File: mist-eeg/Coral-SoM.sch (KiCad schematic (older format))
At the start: 20 parts, among them J5 Extra GPIOs, J6 Digital buses, J7 J1312, J8 J1311, J9 J1310, SW4 RESET, SW5 ONOFF, U9 NX5427001Z

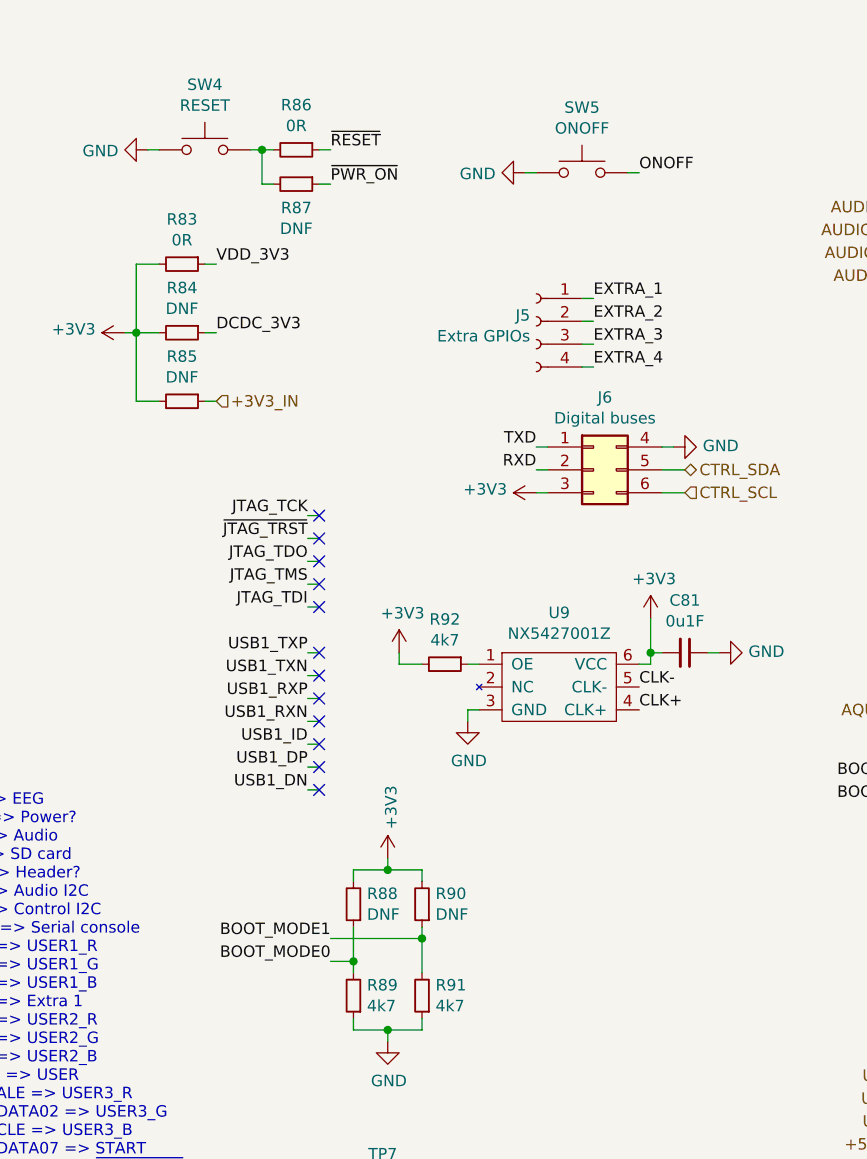
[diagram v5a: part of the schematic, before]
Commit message: Switch to POL switching regulator to accelerate production of the board
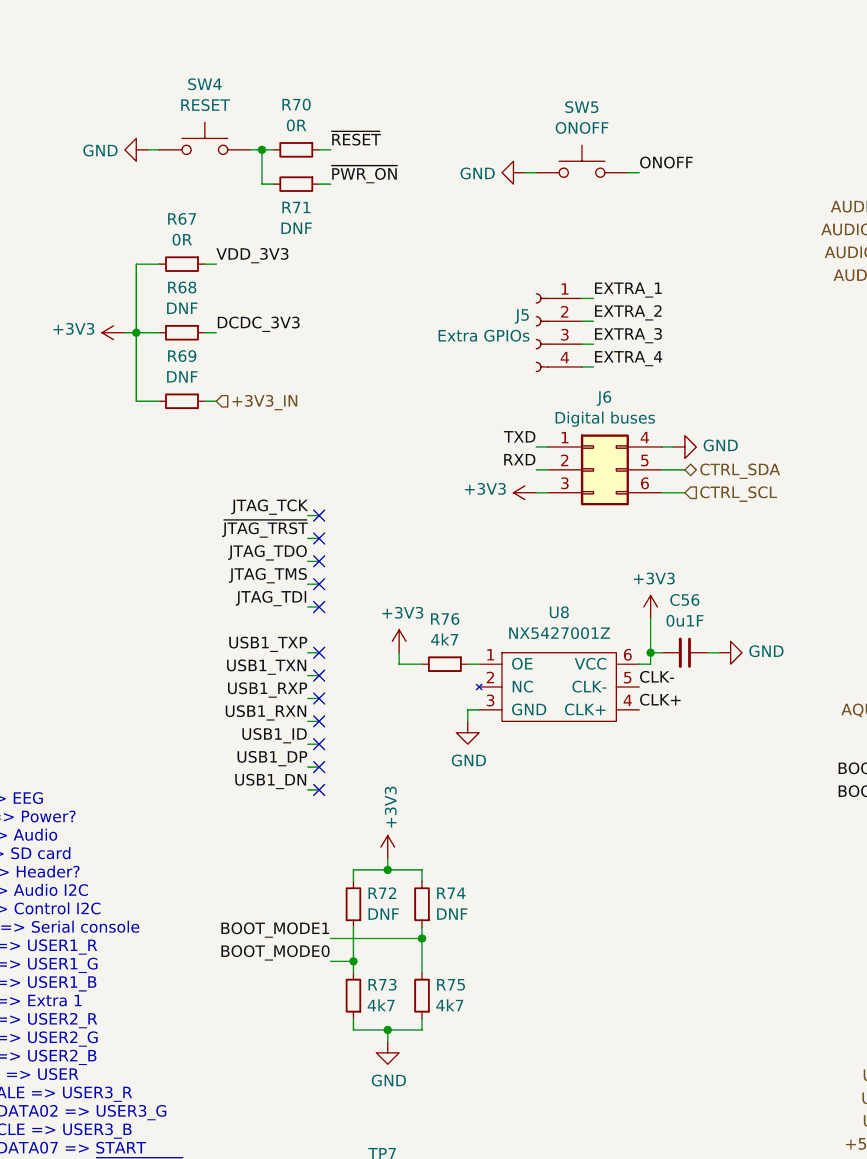
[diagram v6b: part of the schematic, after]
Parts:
- renumbered C81 to C56, R83 to R67, R84 to R68, R85 to R69, R86 to R70, R87 to R71, R88 to R72, R89 to R73, R90 to R74, R91 to R75, R92 to R76, U9 to U8
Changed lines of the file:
@@
 $Descr A4 11693 8268
 encoding utf-8
-Sheet 11 11
+Sheet 11 8
 Title ""
-Date "2021-08-03"
-Rev "1D"
+Date "2021-08-05"
+Rev "1E"
 Comp ""
 Comment1 ""
@@
 $EndComp
 $Comp
-L power:GND #PWR0113
+L power:GND #PWR091
 U 1 1 614447D0
 P 5050 6000
-F 0 "#PWR0113" H 5050 5750 50  0001 C CNN
+F 0 "#PWR091" H 5050 5750 50  0001 C CNN
 F 1 "GND" H 5055 5827 50  0000 C CNN
 F 2 "" H 5050 6000 50  0001 C CNN
@@
 $EndComp
 $Comp
-L power:GND #PWR0114
+L power:GND #PWR092
 U 1 1 61444C99
 P 5450 6000
-F 0 "#PWR0114" H 5450 5750 50  0001 C CNN
+F 0 "#PWR092" H 5450 5750 50  0001 C CNN
 F 1 "GND" H 5455 5827 50  0000 C CNN
 F 2 "" H 5450 6000 50  0001 C CNN
@@
 $EndComp
 $Comp
-L power:GND #PWR0115
+L power:GND #PWR093
 U 1 1 61445116
 P 7050 5950
-F 0 "#PWR0115" H 7050 5700 50  0001 C CNN
+F 0 "#PWR093" H 7050 5700 50  0001 C CNN
 F 1 "GND" H 7055 5777 50  0000 C CNN
 F 2 "" H 7050 5950 50  0001 C CNN
@@
 $EndComp
 $Comp
-L power:GND #PWR0116
+L power:GND #PWR094
 U 1 1 6144559F
 P 7450 5950
-F 0 "#PWR0116" H 7450 5700 50  0001 C CNN
+F 0 "#PWR094" H 7450 5700 50  0001 C CNN
 F 1 "GND" H 7455 5777 50  0000 C CNN
 F 2 "" H 7450 5950 50  0001 C CNN
@@
 $EndComp
 $Comp
-L power:GND #PWR0117
+L power:GND #PWR095
 U 1 1 61445A23
 P 9850 5950
-F 0 "#PWR0117" H 9850 5700 50  0001 C CNN
+F 0 "#PWR095" H 9850 5700 50  0001 C CNN
 F 1 "GND" H 9855 5777 50  0000 C CNN
 F 2 "" H 9850 5950 50  0001 C CNN
@@
 $EndComp
 $Comp
-L power:GND #PWR0118
+L power:GND #PWR096
 U 1 1 61445EC4
 P 10250 5950
-F 0 "#PWR0118" H 10250 5700 50  0001 C CNN
+F 0 "#PWR096" H 10250 5700 50  0001 C CNN
 F 1 "GND" H 10255 5777 50  0000 C CNN
 F 2 "" H 10250 5950 50  0001 C CNN
@@
 Connection ~ 5500 5600
 $Comp
-L power:+3V3 #PWR0102
+L power:+3V3 #PWR080
 U 1 1 615CEE3B
 P 1400 2050
-F 0 "#PWR0102" H 1400 1900 50  0001 C CNN
+F 0 "#PWR080" H 1400 1900 50  0001 C CNN
 F 1 "+3V3" V 1415 2178 50  0000 L CNN
 F 2 "" H 1400 2050 50  0001 C CNN
@@
 P 1500 1250
 AR Path="/60D119DF/616B49C1" Ref="#PWR?"  Part="1"
-AR Path="/61085AB7/616B49C1" Ref="#PWR0103"  Part="1"
-F 0 "#PWR0103" H 1500 1000 50  0001 C CNN
+AR Path="/61085AB7/616B49C1" Ref="#PWR081"  Part="1"
+F 0 "#PWR081" H 1500 1000 50  0001 C CNN
 F 1 "GND" V 1505 1122 50  0000 R CNN
 F 2 "" H 1500 1250 50  0001 C CNN
@@
 +3V3_IN
 $Comp
-L Device:R_Small R83
+L Device:R_Small R67
 U 1 1 60FDBF94
 P 1650 1750
-F 0 "R83" V 1454 1750 50  0000 C CNN
+F 0 "R67" V 1454 1750 50  0000 C CNN
 F 1 "0R" V 1545 1750 50  0000 C CNN
 F 2 "Resistor_SMD:R_0603_1608Metric" H 1650 1750 50  0001 C CNN
@@
 $EndComp
 $Comp
-L Device:R_Small R84
+L Device:R_Small R68
 U 1 1 60FDC090
 P 1650 2050
-F 0 "R84" V 1454 2050 50  0000 C CNN
+F 0 "R68" V 1454 2050 50  0000 C CNN
 F 1 "DNF" V 1545 2050 50  0000 C CNN
 F 2 "Resistor_SMD:R_0603_1608Metric" H 1650 2050 50  0001 C CNN
@@
 $EndComp
 $Comp
-L Device:R_Small R85
+L Device:R_Small R69
 U 1 1 60FDC0FE
 P 1650 2350
-F 0 "R85" V 1454 2350 50  0000 C CNN
+F 0 "R69" V 1454 2350 50  0000 C CNN
 F 1 "DNF" V 1545 2350 50  0000 C CNN
 F 2 "Resistor_SMD:R_0603_1608Metric" H 1650 2350 50  0001 C CNN
@@
 	3200 2750 3250 2750
 $Comp
-L power:+3V3 #PWR0109
+L power:+3V3 #PWR087
 U 1 1 627DB411
 P 3200 2750
-F 0 "#PWR0109" H 3200 2600 50  0001 C CNN
+F 0 "#PWR087" H 3200 2600 50  0001 C CNN
 F 1 "+3V3" V 3215 2878 50  0000 L CNN
 F 2 "" H 3200 2750 50  0001 C CNN
@@
 $EndComp
 $Comp
-L power:GND #PWR0111
+L power:GND #PWR089
 U 1 1 627DBA20
 P 3800 2550
-F 0 "#PWR0111" H 3800 2300 50  0001 C CNN
+F 0 "#PWR089" H 3800 2300 50  0001 C CNN
 F 1 "GND" V 3805 2422 50  0000 R CNN
 F 2 "" H 3800 2550 50  0001 C CNN
@@
 NoConn ~ 9900 2400
 $Comp
-L Device:R_Small R89
+L Device:R_Small R73
 U 1 1 6290419F
 P 2400 4950
-F 0 "R89" H 2341 4904 50  0000 R CNN
+F 0 "R73" H 2341 4904 50  0000 R CNN
 F 1 "4k7" H 2341 4995 50  0000 R CNN
 F 2 "Resistor_SMD:R_0201_0603Metric" H 2400 4950 50  0001 C CNN
@@
 $EndComp
 $Comp
-L Device:R_Small R91
+L Device:R_Small R75
 U 1 1 6290451A
 P 2700 4950
-F 0 "R91" H 2641 4904 50  0000 R CNN
+F 0 "R75" H 2641 4904 50  0000 R CNN
 F 1 "4k7" H 2641 4995 50  0000 R CNN
 F 2 "Resistor_SMD:R_0201_0603Metric" H 2700 4950 50  0001 C CNN
@@
 $EndComp
 $Comp
-L Device:R_Small R90
+L Device:R_Small R74
 U 1 1 62905418
 P 2700 4550
-F 0 "R90" H 2641 4504 50  0000 R CNN
+F 0 "R74" H 2641 4504 50  0000 R CNN
 F 1 "DNF" H 2641 4595 50  0000 R CNN
 F 2 "Resistor_SMD:R_0603_1608Metric" H 2700 4550 50  0001 C CNN
@@
 $EndComp
 $Comp
-L Device:R_Small R88
+L Device:R_Small R72
 U 1 1 62905675
 P 2400 4550
-F 0 "R88" H 2341 4504 50  0000 R CNN
+F 0 "R72" H 2341 4504 50  0000 R CNN
 F 1 "DNF" H 2341 4595 50  0000 R CNN
 F 2 "Resistor_SMD:R_0603_1608Metric" H 2400 4550 50  0001 C CNN
@@
 	2700 4400 2700 4450
 $Comp
-L power:GND #PWR0105
+L power:GND #PWR083
 U 1 1 629D21D1
 P 2550 5150
-F 0 "#PWR0105" H 2550 4900 50  0001 C CNN
+F 0 "#PWR083" H 2550 4900 50  0001 C CNN
 F 1 "GND" H 2555 4977 50  0000 C CNN
 F 2 "" H 2550 5150 50  0001 C CNN
@@
 	2000 1250 2050 1250
 $Comp
-L Device:R_Small R86
+L Device:R_Small R70
 U 1 1 62ADCC1F
 P 2150 1250
-F 0 "R86" V 1954 1250 50  0000 C CNN
+F 0 "R70" V 1954 1250 50  0000 C CNN
 F 1 "0R" V 2045 1250 50  0000 C CNN
 F 2 "Resistor_SMD:R_0603_1608Metric" H 2150 1250 50  0001 C CNN
@@
 $EndComp
 $Comp
-L Device:R_Small R87
+L Device:R_Small R71
 U 1 1 62ADCD0B
 P 2150 1400
-F 0 "R87" V 2254 1400 50  0000 C CNN
+F 0 "R71" V 2254 1400 50  0000 C CNN
 F 1 "DNF" V 2345 1400 50  0000 C CNN
 F 2 "Resistor_SMD:R_0603_1608Metric" H 2150 1400 50  0001 C CNN
@@
 	3650 1350 3600 1350
 $Comp
-L power:GND #PWR0108
+L power:GND #PWR086
 U 1 1 62B8A22D
 P 3150 1350
-F 0 "#PWR0108" H 3150 1100 50  0001 C CNN
+F 0 "#PWR086" H 3150 1100 50  0001 C CNN
 F 1 "GND" V 3155 1222 50  0000 R CNN
 F 2 "" H 3150 1350 50  0001 C CNN
@@
 	3150 1350 3200 1350
 $Comp
-L components:NX5427001Z U9
+L components:NX5427001Z U8
 U 1 1 6103BE94
 P 3250 3600
-F 0 "U9" H 3300 3925 50  0000 C CNN
+F 0 "U8" H 3300 3925 50  0000 C CNN
 F 1 "NX5427001Z" H 3300 3834 50  0000 C CNN
 F 2 "mist-eeg:NX5427001Z" H 3250 3500 50  0001 C CNN
@@
 CLK+
 $Comp
-L power:+3V3 #PWR0110
+L power:+3V3 #PWR088
 U 1 1 610A4550
 P 3700 3300
-F 0 "#PWR0110" H 3700 3150 50  0001 C CNN
+F 0 "#PWR088" H 3700 3150 50  0001 C CNN
 F 1 "+3V3" H 3715 3473 50  0000 C CNN
 F 2 "" H 3700 3300 50  0001 C CNN
@@
 	3700 3500 3650 3500
 $Comp
-L Device:C_Small C81
+L Device:C_Small C56
 U 1 1 610C70CD
 P 3850 3450
-F 0 "C81" V 3621 3450 50  0000 C CNN
+F 0 "C56" V 3621 3450 50  0000 C CNN
 F 1 "0u1F" V 3712 3450 50  0000 C CNN
 F 2 "Capacitor_SMD:C_0201_0603Metric" H 3850 3450 50  0001 C CNN
@@
 	3700 3450 3700 3500
 $Comp
-L power:GND #PWR0112
+L power:GND #PWR090
 U 1 1 610E9DBB
 P 4000 3450
-F 0 "#PWR0112" H 4000 3200 50  0001 C CNN
+F 0 "#PWR090" H 4000 3200 50  0001 C CNN
 F 1 "GND" V 4005 3322 50  0000 R CNN
 F 2 "" H 4000 3450 50  0001 C CNN
@@
 	4000 3450 3950 3450
 $Comp
-L power:GND #PWR0107
+L power:GND #PWR085
 U 1 1 611314F6
 P 2900 3750
-F 0 "#PWR0107" H 2900 3500 50  0001 C CNN
+F 0 "#PWR085" H 2900 3500 50  0001 C CNN
 F 1 "GND" H 2905 3577 50  0000 C CNN
 F 2 "" H 2900 3750 50  0001 C CNN
@@
 	2900 3700 2950 3700
 $Comp
-L Device:R_Small R92
+L Device:R_Small R76
 U 1 1 61156BB0
 P 2800 3500
-F 0 "R92" V 2604 3500 50  0000 C CNN
+F 0 "R76" V 2604 3500 50  0000 C CNN
 F 1 "4k7" V 2695 3500 50  0000 C CNN
 F 2 "Resistor_SMD:R_0201_0603Metric" H 2800 3500 50  0001 C CNN
@@
 $EndComp
 $Comp
-L power:+3V3 #PWR0106
+L power:+3V3 #PWR084
 U 1 1 61157269
 P 2600 3450
-F 0 "#PWR0106" H 2600 3300 50  0001 C CNN
+F 0 "#PWR084" H 2600 3300 50  0001 C CNN
 F 1 "+3V3" H 2615 3623 50  0000 C CNN
 F 2 "" H 2600 3450 50  0001 C CNN
@@
 	2600 3500 2700 3500
 $Comp
-L power:+3V3 #PWR0104
+L power:+3V3 #PWR082
 U 1 1 6104B8C8
 P 2550 4350
-F 0 "#PWR0104" H 2550 4200 50  0001 C CNN
+F 0 "#PWR082" H 2550 4200 50  0001 C CNN
 F 1 "+3V3" V 2565 4478 50  0000 L CNN
 F 2 "" H 2550 4350 50  0001 C CNN
